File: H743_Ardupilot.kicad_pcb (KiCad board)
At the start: 6 copper layers, 36.5 x 36.5 mm, 156 parts, among them J1 Analog, J10 Led ext, J11 Buzzer, J12 10067099-200LF, J13 Can1_2, J14 Can1_1, J2 Uart1, J3 Uart4, J4 Uart7, J5 Uart(, J6 Uart6, J7 Uart3, J8 I2C1, J9 I2C_2, Q1 AO3400A, U1 USBLC6-2P6, U10 LSM6DSV16X, U11 ICM-45686, U12 BMP581, U13 DPS368XTSA1, U14 SM08B-SRSS-TB(LF)(SN), U2 STM32H743VIT6, U3 LMR43620R5RPER, U4 LMR604303SRAKRQ1, U5 AP7361C-33FGE-7, U6 AP7361C-33FGE-7, U7 TJA1051TK/3,118, U8 SM04B-GHS-TB(LF)(SN), U9 BMI088, Y1 8MHz

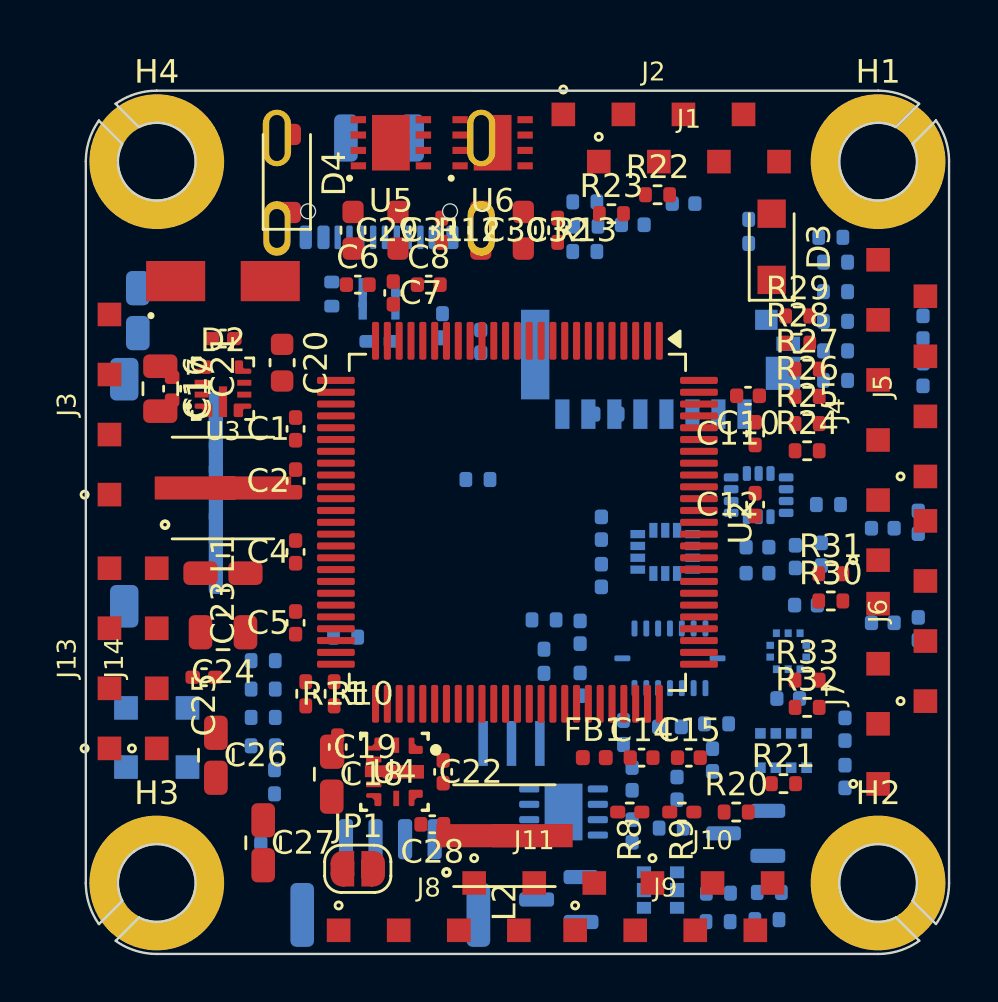
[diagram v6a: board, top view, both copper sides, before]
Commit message: Add inner GND planes and perimeter stitching vias
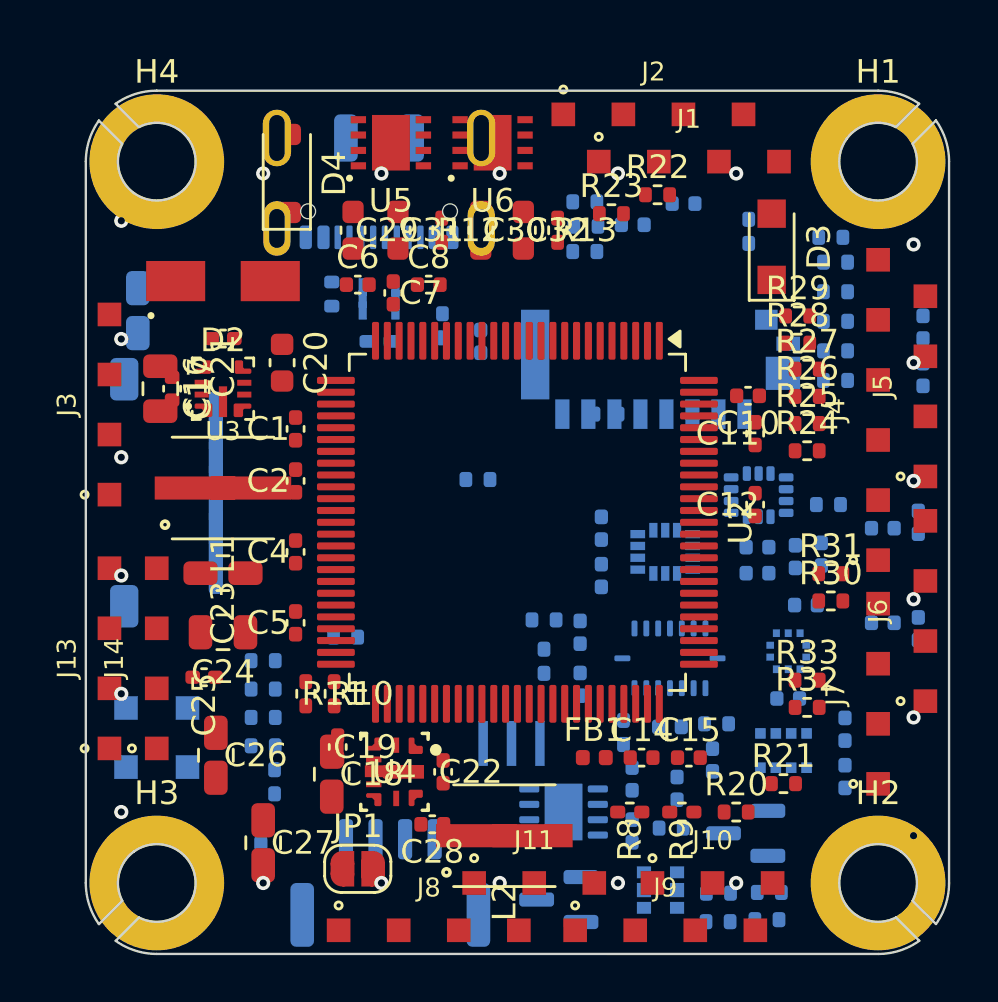
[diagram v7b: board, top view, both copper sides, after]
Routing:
- net GND: vias 0 -> 26
- added copper zone on In1.Cu, net GND
- added copper zone on In4.Cu, net GND
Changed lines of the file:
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@@
 	)
 	(embedded_fonts no)
+	(zone
+		(net "GND")
+		(net_name "GND")
+		(layer "In1.Cu")
+		(hatch edge 0.5)
+		(connect_pads (clearance 0.2))
+		(min_thickness 0.2)
+		(fill yes (thermal_gap 0.3) (thermal_bridge_width 0.3))
+		(polygon (pts (xy 76 88) (xy 110 88) (xy 110 119.5) (xy 76 119.5)))
+	)
+	(zone
+		(net "GND")
+		(net_name "GND")
+		(layer "In4.Cu")
+		(hatch edge 0.5)
+		(connect_pads (clearance 0.2))
+		(min_thickness 0.2)
+		(fill yes (thermal_gap 0.3) (thermal_bridge_width 0.3))
+		(polygon (pts (xy 76 88) (xy 110 88) (xy 110 119.5) (xy 76 119.5)))
+	)
+	(via (at 77 89) (size 0.6) (drill 0.3) (layers "F.Cu" "B.Cu") (net "GND"))
+	(via (at 82 89) (size 0.6) (drill 0.3) (layers "F.Cu" "B.Cu") (net "GND"))
+	(via (at 87 89) (size 0.6) (drill 0.3) (layers "F.Cu" "B.Cu") (net "GND"))
+	(via (at 92 89) (size 0.6) (drill 0.3) (layers "F.Cu" "B.Cu") (net "GND"))
+	(via (at 97 89) (size 0.6) (drill 0.3) (layers "F.Cu" "B.Cu") (net "GND"))
+	(via (at 102 89) (size 0.6) (drill 0.3) (layers "F.Cu" "B.Cu") (net "GND"))
+	(via (at 107 89) (size 0.6) (drill 0.3) (layers "F.Cu" "B.Cu") (net "GND"))
+	(via (at 109.5 92) (size 0.6) (drill 0.3) (layers "F.Cu" "B.Cu") (net "GND"))
+	(via (at 109.5 97) (size 0.6) (drill 0.3) (layers "F.Cu" "B.Cu") (net "GND"))
+	(via (at 109.5 102) (size 0.6) (drill 0.3) (layers "F.Cu" "B.Cu") (net "GND"))
+	(via (at 109.5 107) (size 0.6) (drill 0.3) (layers "F.Cu" "B.Cu") (net "GND"))
+	(via (at 109.5 112) (size 0.6) (drill 0.3) (layers "F.Cu" "B.Cu") (net "GND"))
+	(via (at 109.5 117) (size 0.6) (drill 0.3) (layers "F.Cu" "B.Cu") (net "GND"))
+	(via (at 107 119) (size 0.6) (drill 0.3) (layers "F.Cu" "B.Cu") (net "GND"))
+	(via (at 102 119) (size 0.6) (drill 0.3) (layers "F.Cu" "B.Cu") (net "GND"))
+	(via (at 97 119) (size 0.6) (drill 0.3) (layers "F.Cu" "B.Cu") (net "GND"))
+	(via (at 92 119) (size 0.6) (drill 0.3) (layers "F.Cu" "B.Cu") (net "GND"))
+	(via (at 87 119) (size 0.6) (drill 0.3) (layers "F.Cu" "B.Cu") (net "GND"))
+	(via (at 82 119) (size 0.6) (drill 0.3) (layers "F.Cu" "B.Cu") (net "GND"))
+	(via (at 77 119) (size 0.6) (drill 0.3) (layers "F.Cu" "B.Cu") (net "GND"))
+	(via (at 76 116) (size 0.6) (drill 0.3) (layers "F.Cu" "B.Cu") (net "GND"))
+	(via (at 76 111) (size 0.6) (drill 0.3) (layers "F.Cu" "B.Cu") (net "GND"))
+	(via (at 76 106) (size 0.6) (drill 0.3) (layers "F.Cu" "B.Cu") (net "GND"))
+	(via (at 76 101) (size 0.6) (drill 0.3) (layers "F.Cu" "B.Cu") (net "GND"))
+	(via (at 76 96) (size 0.6) (drill 0.3) (layers "F.Cu" "B.Cu") (net "GND"))
+	(via (at 76 91) (size 0.6) (drill 0.3) (layers "F.Cu" "B.Cu") (net "GND"))
 )

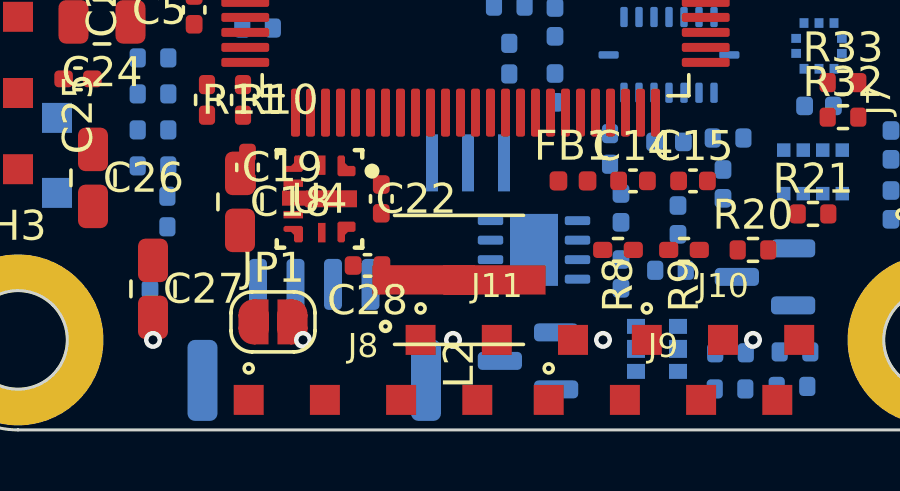
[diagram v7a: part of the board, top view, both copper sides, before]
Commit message: Fix SDIO resistor reference and improve 9V inductor isolation
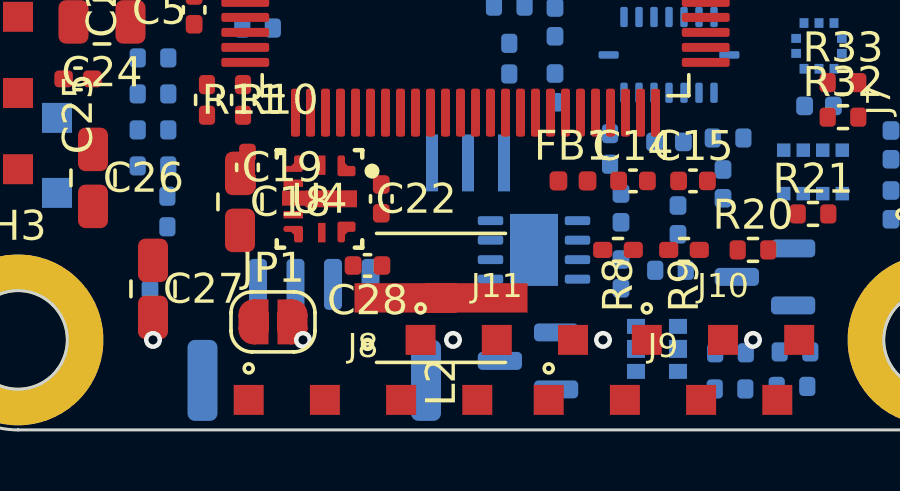
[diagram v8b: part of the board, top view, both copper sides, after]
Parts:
- moved L2 0.85 mm to (91.6, 117.6)
- renumbered R47 to R51
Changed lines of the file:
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@@
 	(footprint "H743_Custom:L_Coilcraft_XGL4030"
 		(layer "F.Cu")
-		(at 92.2 117 0)
+		(at 91.6 117.6 0)
 		(descr "Coilcraft XGL4030 shielded power inductor; recommended land pattern for Coilcraft XGL4030 series, 4.0 x 4.0 mm body")
 		(tags "Coilcraft XGL4030 power inductor 4x4mm")
@@
 		(descr "Resistor SMD 0402 (1005 Metric), square (rectangular) end terminal, IPC-7351 nominal, (Body size source: IPC-SM-782 page 72, https://www.pcb-3d.com/wordpress/wp-content/uploads/ipc-sm-782a_amendment_1_and_2.pdf)")
 		(tags "resistor")
-		(property "Reference" "R47"
+		(property "Reference" "R51"
 			(at 0 1.17 0)
 			(layer "B.SilkS")
